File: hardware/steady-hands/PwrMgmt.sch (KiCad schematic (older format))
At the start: 35 parts, among them J5 USB_B_Micro, J6 BATT, SW3 PWR_SW, U6 BQ24075, U7 TPS62841DGR, U8 TPS63001

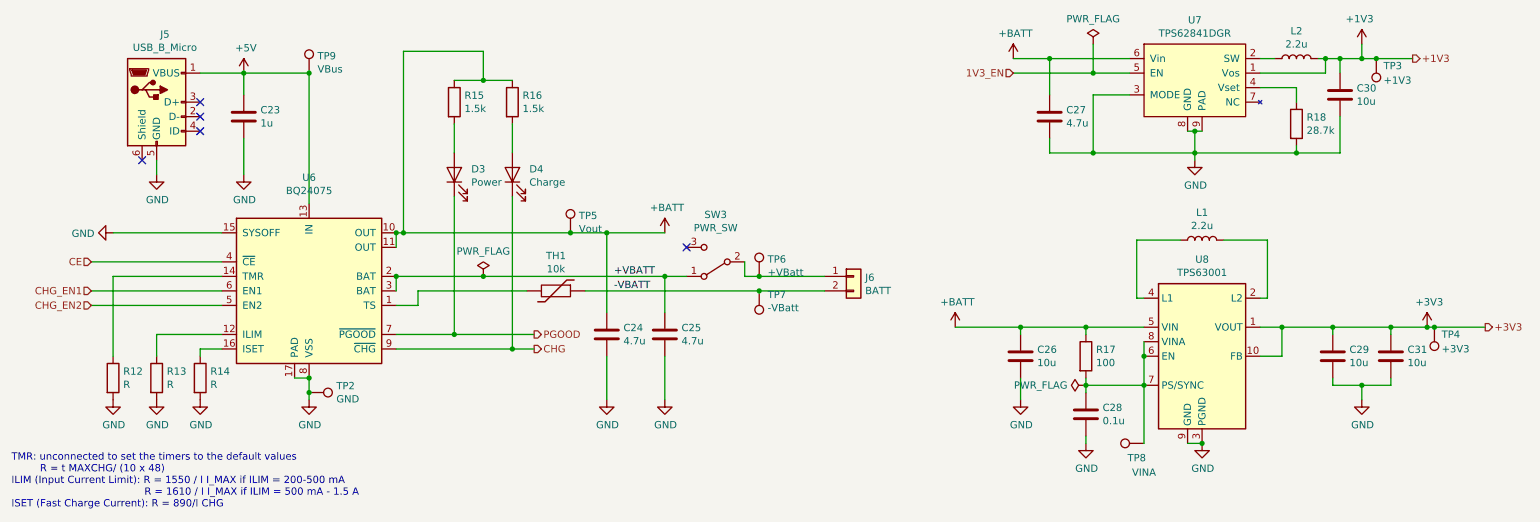
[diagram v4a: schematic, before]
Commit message: Edits PCB layout
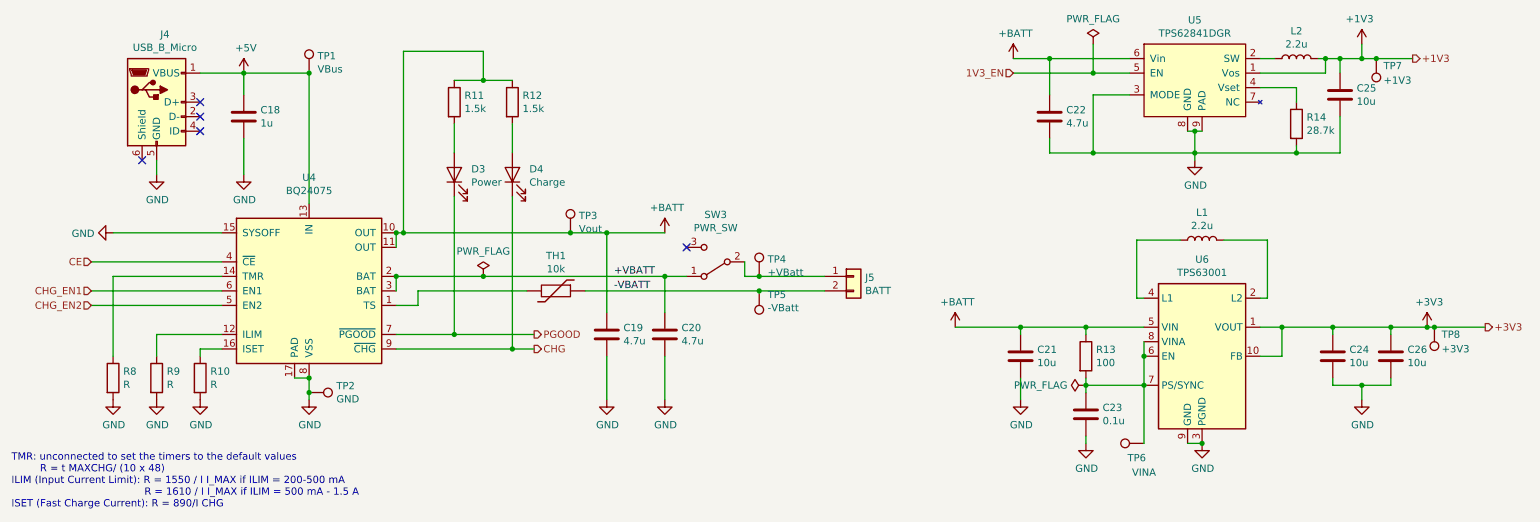
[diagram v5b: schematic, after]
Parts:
- renumbered C23 to C18, C24 to C19, C25 to C20, C26 to C21, C27 to C22, C28 to C23, C29 to C24, C30 to C25, C31 to C26, J5 to J4, J6 to J5, R14 to R10, R15 to R11, R16 to R12, R17 to R13, R18 to R14, R12 to R8, R13 to R9, TP9 to TP1, TP5 to TP3, TP6 to TP4, TP7 to TP5, TP8 to TP6, TP3 to TP7, TP4 to TP8, U6 to U4, U7 to U5, U8 to U6
